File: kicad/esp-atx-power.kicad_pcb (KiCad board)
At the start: 4 copper layers, 44.7 x 42.6 mm, 73 parts, among them J101 Conn_02x02_Odd_Even, J102 Conn_02x02_Odd_Even, J103 Conn_02x02_Odd_Even, J104 Conn_02x02_Odd_Even, J105 GT-USB-7010ASV, K101 G3VM-61D1, K102 G3VM-61D1, K103 G3VM-61D1, K104 G3VM-61D1, Q101 SS8050, Q102 SS8050, SW101 TS-1187A-B-A-B, SW102 TS-1187A-B-A-B, U102 LD1117S33CTR, U103 USBLC6-2P6, U104 CP2102-GMR, U201 ESP32-S2FH4, Y201 40MHz

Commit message: Fix RTS/DTR and increase LEDs resistors
- RTS/DTR has been inverted and RTS assertin doesn't reset the board.
- Increase the LED resistors to decrease brightness
- Change JLCPCB order number position
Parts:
- R114: value 100 -> 200
- R115: value 10 -> 22
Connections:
- Q101 pad 2: DTR -> RTS
- Q102 pad 2: RTS -> DTR
- R108 pad 1: RTS -> DTR
- R109 pad 1: DTR -> RTS
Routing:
- net DTR: track 41.1 -> 41.8 mm
- net +3V3: track 176.8 -> 177.4 mm
- net GND: vias 277 -> 279
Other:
- board text added: "ESP32 ATX Power Controller Revision 1.0.1"
- board text removed: "ESP32 ATX Power Controller Revision 1.0.0"

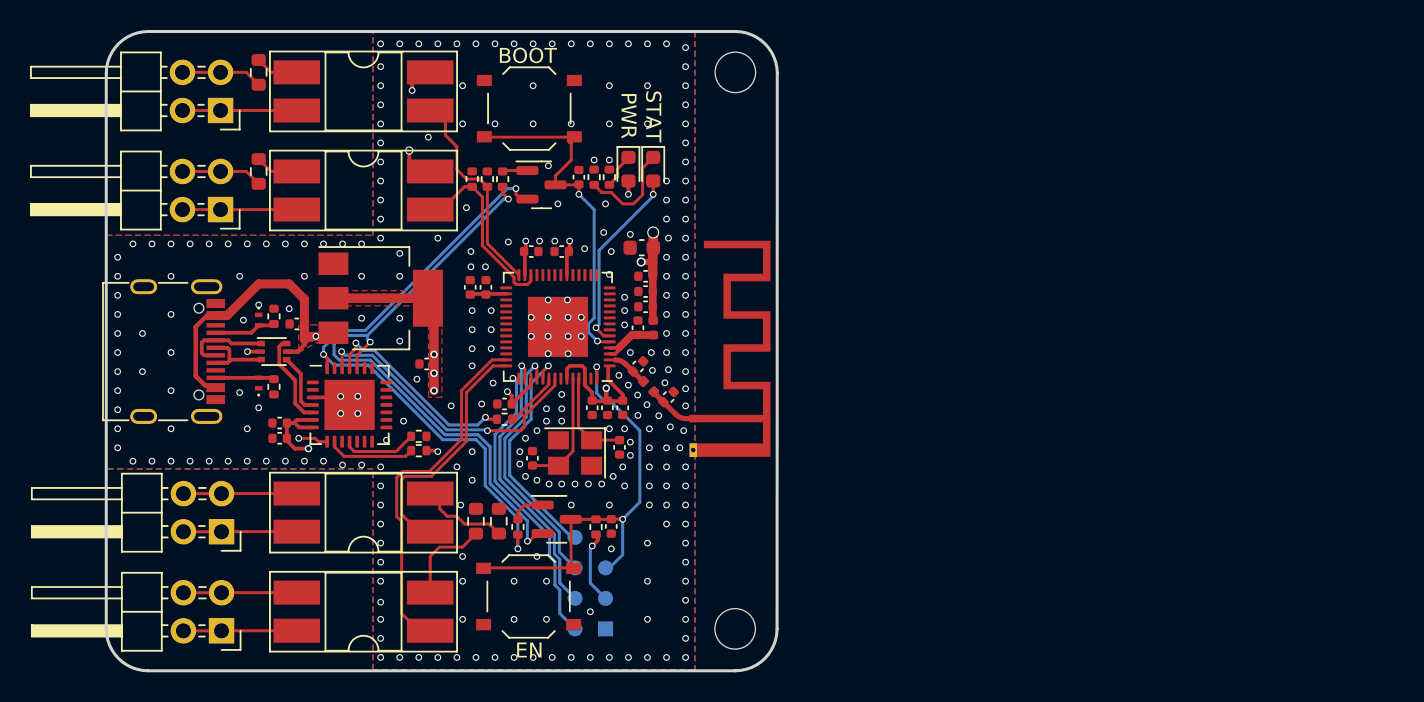
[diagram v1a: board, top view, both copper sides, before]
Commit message: Update board form factor and change ESP module
- PCB antenna is not well working inside computer casing
- Select an ESP with external antenna connector
- Remove USB-UART bridge which is no longer required for flashing
- Use on unique pin header instead of 4
- Add 5V external power supply in case USB port is not available
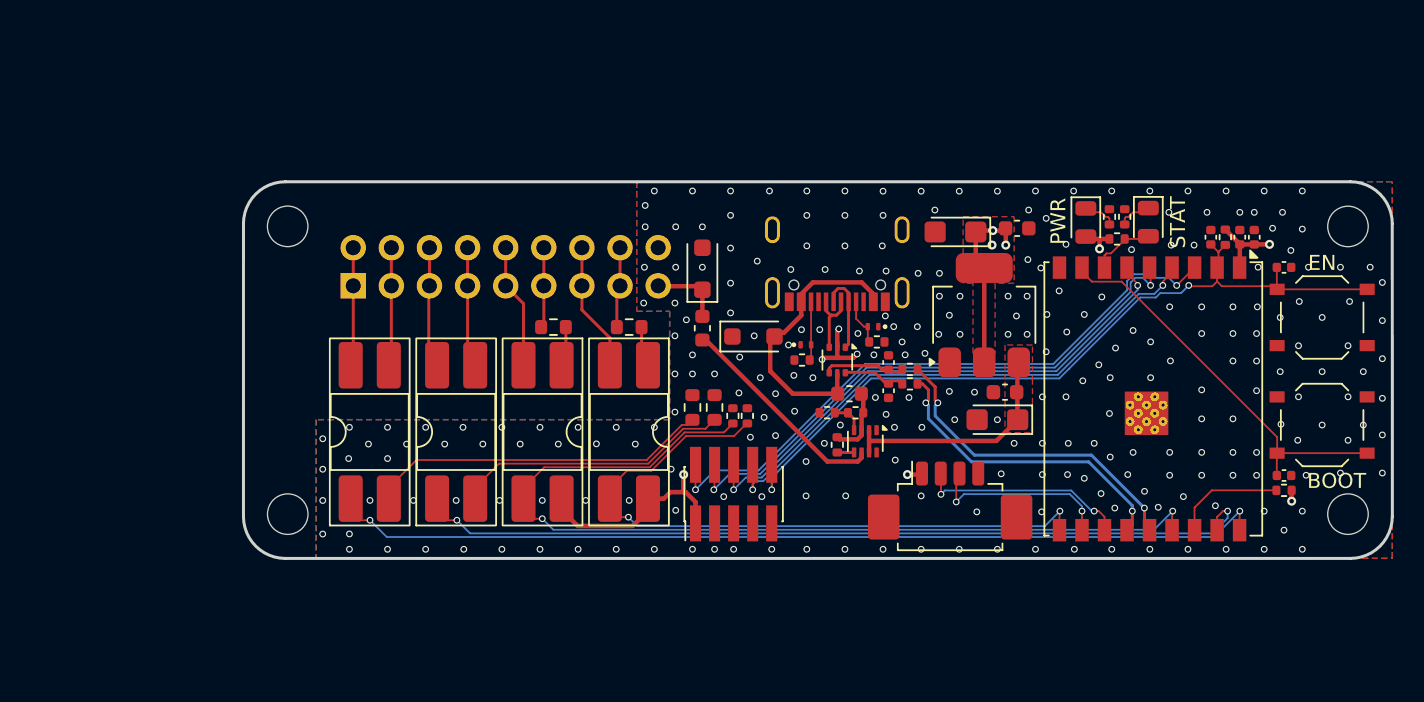
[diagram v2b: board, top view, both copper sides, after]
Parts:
- removed AE201: Antenna_Chip, RF_Antenna:Texas_SWRA117D_2.4GHz_Left
- removed C201, C211: 100p, Capacitor_SMD:C_0402_1005Metric
- removed C202, C206, C207, C208, C209, C212: 100n, Capacitor_SMD:C_0402_1005Metric
- removed C203, C210, C213: 1u, Capacitor_SMD:C_0402_1005Metric
- removed C204: 10u, Capacitor_SMD:C_0402_1005Metric
- removed C205: 22u, Capacitor_SMD:C_0603_1608Metric
- removed C214, C215: 12p, Capacitor_SMD:C_0402_1005Metric
- removed C216, C217: 1.8p, Capacitor_SMD:C_0402_1005Metric
- removed J104: Conn_02x02_Odd_Even, Connector_PinHeader_2.54mm:PinHeader_2x02_P2.54mm_Horizontal
- removed L201: 2n, Inductor_SMD:L_0402_1005Metric
- removed L202: 2.5n, Inductor_SMD:L_0402_1005Metric
- removed Q101, Q102: SS8050, Package_TO_SOT_SMD:SOT-23
- removed R201: 470, Resistor_SMD:R_0402_1005Metric
- removed TP201: GND, TestPoint:TestPoint_Pad_1.0x1.0mm
- removed TP202: 3V3, TestPoint:TestPoint_Pad_D1.0mm
- removed TP203: RST, TestPoint:TestPoint_Pad_D1.0mm
- removed TP204: TCK, TestPoint:TestPoint_Pad_D1.0mm
- removed TP205: TDO, TestPoint:TestPoint_Pad_D1.0mm
- removed TP206: TDI, TestPoint:TestPoint_Pad_D1.0mm
- removed TP207: TMS, TestPoint:TestPoint_Pad_D1.0mm
- removed U201: ESP32-S2FH4, Package_DFN_QFN:QFN-56-1EP_7x7mm_P0.4mm_EP4x4mm
- removed Y201: 40MHz, Crystal:Crystal_SMD_3225-4Pin_3.2x2.5mm
- added C101: 100n, Capacitor_SMD:C_0402_1005Metric, F.Cu at (183.2, 100.5)
- added C102: 10u, Capacitor_SMD:C_0402_1005Metric, F.Cu at (184.2, 100.5)
- added C109: ~, Capacitor_SMD:C_0402_1005Metric, F.Cu at (159.8, 108.9)
- added C110: 100n, Capacitor_SMD:C_0603_1608Metric, F.Cu at (168.4, 99.9)
- added C111: 10u, Capacitor_Tantalum_SMD:CP_EIA-3216-18_Kemet-A, F.Cu at (167.1, 112.7)
- added D105: SMF5.0A, Diode_SMD:D_SOD-123F, F.Cu at (147.4, 102.6)
- added D106: SMF5.0A, Diode_SMD:D_SOD-123F, F.Cu at (150.8, 107.1)
- added L101: Ferrite Bead, Inductor_SMD:L_0603_1608Metric, F.Cu at (157.2, 110.9)
- added L102: Ferrite Bead, Inductor_SMD:L_0603_1608Metric, F.Cu at (147.4, 106.6)
- added MH103: ~, MountingHole:MountingHole_2.7mm_M2.5_ISO7380, F.Cu at (190.4, 119.0)
- added MH104: ~, MountingHole:MountingHole_2.7mm_M2.5_ISO7380, F.Cu at (119.8, 119.0)
- added R116: 0, Resistor_SMD:R_0402_1005Metric, F.Cu at (156.4, 114.4)
- added R117: 10k, Resistor_SMD:R_0402_1005Metric, F.Cu at (157.6, 112.2)
- added R118: 10k, Resistor_SMD:R_0402_1005Metric, F.Cu at (155.7, 112.2)
- added U101: ESP32-C3-WROOM-02U, RF_Module:ESP32-C3-WROOM-02U, F.Cu at (177.2, 111.3)
- C103: footprint Capacitor_SMD:C_0402_1005Metric -> Capacitor_SMD:C_0603_1608Metric
- C104: footprint Capacitor_SMD:C_0402_1005Metric -> Capacitor_Tantalum_SMD:CP_EIA-3216-18_Kemet-A
- C107: value 4.7u -> 1u
- C108: value 100n -> ~
- D103, D104: footprint LED_SMD:LED_0603_1608Metric -> LED_SMD:LED_0805_2012Metric
- J101: value Conn_02x02_Odd_Even -> Conn_ARM_JTAG_SWD_10; footprint Connector_PinHeader_2.54mm:PinHeader_2x02_P2.54mm_Horizontal -> Connector_PinHeader_1.27mm:PinHeader_2x05_P1.27mm_Vertical_SMD
- J102: value Conn_02x02_Odd_Even -> Conn_02x09_Odd_Even; footprint Connector_PinHeader_2.54mm:PinHeader_2x02_P2.54mm_Horizontal -> Connector_PinHeader_2.54mm:PinHeader_2x09_P2.54mm_Horizontal
- J103: value Conn_02x02_Odd_Even -> Conn_01x04; footprint Connector_PinHeader_2.54mm:PinHeader_2x02_P2.54mm_Horizontal -> Connector_Molex:Molex_PicoBlade_53261-0471_1x04-1MP_P1.25mm_Horizontal
- R112, R113: value 10k -> 22
- R114: value 200 -> 680
- R115: value 22 -> 680
- U102: value LD1117S33CTR -> AMS1117-3.3
- U104: value CP2102-GMR -> TPS2116DRL; footprint Package_DFN_QFN:QFN-28-1EP_5x5mm_P0.5mm_EP3.35x3.35mm -> Package_TO_SOT_SMD:SOT-583-8
- moved C107 63.5 mm to (181.3, 100.5), turned to 90 degrees
- moved SW102 56.9 mm to (188.7, 113.0)
- moved SW101 56.1 mm to (188.7, 105.9)
- moved J103 52.6 mm to (163.9, 118.7), turned to 0 degrees
- moved R108 51.1 mm to (186.2, 117.4), turned to 0 degrees
- moved C106 51.0 mm to (186.2, 116.4), turned to 0 degrees
- moved MH102 48.9 mm to (190.4, 99.8)
- moved C105 48.0 mm to (186.2, 102.5), turned to 0 degrees
- moved C103 47.4 mm to (167.6, 110.8)
- moved R103 46.2 mm to (182.3, 100.5), turned to 90 degrees
- moved J105 45.7 mm to (156.4, 101.1), turned to 180 degrees
- moved R109 41.1 mm to (175.1, 100.6), turned to 180 degrees
- moved D101 40.9 mm to (158.8, 106.5), turned to 180 degrees
- moved C108 40.6 mm to (159.8, 110.7), turned to -90 degrees
- moved U102 40.2 mm to (166.2, 105.7), turned to 90 degrees
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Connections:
- net BOOT renamed /BOOT
- net HDD_LED renamed /HDD_LED
- net PWR_LED renamed /PWR_LED
- C103 pad 1: VBUS -> +5V
- C105 pad 1: EN -> /EN
- C107 pad 1: +3V3 -> /EN
- C108 pad 1: +3V3 -> /USB_DN
- D104 pad 2: STATUS -> /STATUS
- J101 pad 1: Net-(J101-Pin_1) -> +3V3
- J101 pad 2: Net-(J101-Pin_1) -> /TMS
- J101 pad 3: Net-(J101-Pin_3) -> GND
- J101 pad 4: Net-(J101-Pin_3) -> /TCK
- J102 pad 1: Net-(J102-Pin_1) -> /PWR_SW_P
- J102 pad 2: Net-(J102-Pin_1) -> /PWR_SW_P
- J102 pad 3: Net-(J102-Pin_3) -> /PWR_SW_N
- J102 pad 4: Net-(J102-Pin_3) -> /PWR_SW_N
- J103 pad 1: Net-(J103-Pin_1) -> +3V3
- J103 pad 2: Net-(J103-Pin_1) -> /TX
- J103 pad 3: Net-(J103-Pin_3) -> /RX
- J103 pad 4: Net-(J103-Pin_3) -> GND
- K101 pad 1: PWR_SW -> /PWR_SW
- K101 pad 3: Net-(J101-Pin_3) -> /PWR_SW_N
- K101 pad 4: Net-(J101-Pin_1) -> /PWR_SW_P
- K102 pad 1: RST_SW -> /RST_SW
- K102 pad 3: Net-(J102-Pin_3) -> /RST_SW_N
- K102 pad 4: Net-(J102-Pin_1) -> /RST_SW_P
- K103 pad 2: Net-(J103-Pin_1) -> /PWR_LED_N
- K104 pad 2: Net-(J104-Pin_1) -> /HDD_LED_N
- R103 pad 1: EN -> /EN
- R104 pad 2: Net-(J103-Pin_3) -> /PWR_LED_P
- R106 pad 2: Net-(J104-Pin_3) -> /HDD_LED_P
- R108 pad 1: DTR -> Net-(U101-IO2)
- R108 pad 2: Net-(Q101-B) -> +3V3
- R109 pad 1: RTS -> /STATUS
- R109 pad 2: Net-(Q102-B) -> +3V3
- R112 pad 1: Net-(U104-~{SUSPEND}) -> /USB_DN
- R112 pad 2: GND -> /USB_EDN
- R113 pad 1: Net-(U104-~{RST}) -> /USB_DP
- R113 pad 2: +3V3 -> /USB_EDP
- SW101 pad 1: EN -> /EN
- U102 pad 3: VBUS -> +5V
- U103 pad 4: USB_DP -> /USB_DP
- U103 pad 6: USB_DN -> /USB_DN
- U104 pad 1: unconnected-(U104-~{DCD}-Pad1) -> GND
- U104 pad 2: unconnected-(U104-~{RI}/CLK-Pad2) -> +5V
- U104 pad 3: GND -> Net-(U104-VIN1)
- U104 pad 4: USB_DP -> Net-(U104-PR1)
- U104 pad 5: USB_DN -> Net-(U104-MODE)
- U104 pad 6: +3V3 -> Net-(U104-VIN2)
- U104 pad 7: +3V3 -> +5V
- U104 pad 8: VBUS -> unconnected-(U104-ST-Pad8)
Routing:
- net /PWR_SW: track 0.00 -> 63.2 mm, vias 0 -> 2
- net +3V3: track 177.4 -> 118.5 mm, vias 15 -> 8
- net /RST_SW: track 0.00 -> 56.7 mm, vias 0 -> 2
- net /EN: track 0.00 -> 52.5 mm, vias 0 -> 2
- net /PWR_LED: track 12.6 -> 62.7 mm, vias 0 -> 2
- net /TMS: track 0.00 -> 42.0 mm, vias 0 -> 2
- net DTR: track 41.8 -> 0.00 mm, vias 3 -> 0
- net RTS: track 41.4 -> 0.00 mm, vias 3 -> 0
- net /TCK: track 0.00 -> 38.5 mm, vias 0 -> 2
- net /TDI: track 0.00 -> 36.3 mm, vias 0 -> 2
- net /TDO: track 0.00 -> 35.9 mm, vias 0 -> 2
- net /HDD_LED: track 14.5 -> 44.4 mm, vias 0 -> 2
- net EN: track 29.3 -> 0.00 mm, vias 2 -> 0
- net PWR_SW: track 24.0 -> 0.00 mm
- net /USB_EDP: track 0.00 -> 21.8 mm, vias 0 -> 2
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- added copper zone on F.Cu, net +5V
- removed copper zone on F.Cu, net VBUS
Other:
- board size 44.7 x 42.6 mm -> 76.6 x 25.1 mm
- rule pad_to_mask_clearance: 0 -> 0.05
- board text added: "-"
- board text added: "5V"
- board text added: "76.7612 mm x 25.1992 mm"
- board text added: "ESP32 ATX Power Controller Revision 2.0.0"
- board text added: "RX"
- board text added: "TX"
- board text added: "x"
- board text removed: "44.7180 mm x 42.6013 mm"
- board text removed: "ESP32 ATX Power Controller Revision 1.0.1"

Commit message: Fix TVS diode orientation
The selected diode was not bidirectional, update schematic symbol
to take it into account and fix orientation on VBUS (short circuit).
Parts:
- turned D106 to 180 degrees
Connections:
- D106 pad 1: GND -> VBUS
- D106 pad 2: VBUS -> GND
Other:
- board text added: "ESP32 ATX Power Controller Revision 2.0.1"
- board text removed: "ESP32 ATX Power Controller Revision 2.0.0"

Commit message: Update obsolete components
- G3VM-61D1 is obselete and not manufactured anymore. A similar
reference has been set with smaller package
- Molex connector for debug is not available on JLCPCB anymore.
Alternative found with similar footprint
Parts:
- K101, K102, K103, K104: value G3VM-61D1 -> G3VM-61VY3; footprint Package_DIP:DIP-4_W8.89mm_SMDSocket_LongPads -> Package_SO:SOP-4_3.8x4.1mm_P2.54mm
- moved K104 2.11 mm to (140.8, 112.3)
- moved K103 1.61 mm to (135.7, 112.3)
- moved K102 1.29 mm to (130.5, 112.3)
- moved K101 1.18 mm to (125.4, 112.3)
- moved R104 0.79 mm to (136.9, 107.1), turned to 90 degrees
- moved R106 0.75 mm to (142.0, 107.1), turned to 90 degrees
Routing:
- net /HDD_LED: track 44.4 -> 51.3 mm, vias 2 -> 3
- net /PWR_LED: track 62.7 -> 68.1 mm, vias 2 -> 3
- net /RST_SW: track 56.7 -> 60.1 mm
- net /PWR_SW: track 63.2 -> 65.4 mm
- net Net-(K102-K): track 18.6 -> 20.8 mm, vias 0 -> 2
- net +3V3: track 118.5 -> 120.6 mm, vias 8 -> 10
- net Net-(K101-K): track 22.8 -> 24.0 mm, vias 0 -> 2
- net Net-(K104-A): track 2.73 -> 1.69 mm
- net Net-(K103-A): track 2.66 -> 1.69 mm
- net GND: vias 269 -> 266
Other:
- board text added: "ESP32 ATX Power Controller Revision 2.1.0"
- board text removed: "ESP32 ATX Power Controller Revision 2.0.1"
